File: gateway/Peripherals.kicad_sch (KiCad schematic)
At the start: 11 parts, among them X1101 I2C, X1102 I2C

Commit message: Working on version 1.0
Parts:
- C1101, C1102: footprint Capacitor_SMD:C_0402_1005Metric -> Capacitor_SMD:C_0805_2012Metric; manf# 04025C104JAT2A -> 08053C104M4T4A; mouser# (none) -> 581-08053C104M4T4A
- R1101: footprint (none) -> Resistor_SMD:R_0805_2012Metric; manf (none) -> Bourns; manf# (none) -> CR0805-FX-1001GLF; mouser# (none) -> 652-CR0805-FX-1001GLF
- R1102: footprint (none) -> Resistor_SMD:R_0805_2012Metric; manf (none) -> Bourns; manf# (none) -> CR0805-JW-103GLF; mouser# (none) -> 652-CR0805-JW-103GLF
- TP1101: footprint (none) -> Testpoints_Kampi:TestPoint_Pad_1.0x1.0mm
- X1101: renamed from X?; footprint (none) -> Connector_USB:USB_C_Receptacle_GCT_USB4110; manf (none) -> GCT; manf# (none) -> USB4110-GF-A; mouser# (none) -> 640-USB4110-GF-A
- X1102: renamed from X?; now left out of the parts list
- X1103: renamed from X1101; now left out of the parts list
- X1104: renamed from X1102; now left out of the parts list
- gave numbers to parts that had none: 2

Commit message: Working on PCB
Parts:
- X1103, X1104: footprint (none) -> Connector_PinHeader_2.54mm:PinHeader_1x02_P2.54mm_Vertical
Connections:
- net GPIO.Num0: now reaches X1102.2 (Pin_2)
- net GPIO.Num1: now reaches X1102.3 (Pin_3)
- net GPIO.Num2: now reaches X1102.4 (Pin_4)
- net GPIO.Num3: now reaches X1102.5 (Pin_5)
- net GPIO.Num4: now reaches X1102.6 (Pin_6)
- net GPIO.Num5: now reaches X1102.7 (Pin_7)
- net GPIO.Num6: now reaches X1102.8 (Pin_8)
- net GPIO.Num7: now reaches X1102.9 (Pin_9)
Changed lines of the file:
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@@
 	)
 	(bus_entry
-		(at 363.22 90.17)
+		(at 355.6 90.17)
 		(size 2.54 2.54)
 		(stroke
@@
 	)
 	(bus_entry
-		(at 363.22 85.09)
+		(at 355.6 85.09)
 		(size 2.54 2.54)
 		(stroke
@@
 	)
 	(bus_entry
-		(at 363.22 87.63)
+		(at 355.6 87.63)
 		(size 2.54 2.54)
 		(stroke
@@
 	)
 	(bus_entry
-		(at 363.22 74.93)
+		(at 355.6 74.93)
 		(size 2.54 2.54)
 		(stroke
@@
 	)
 	(bus_entry
-		(at 363.22 77.47)
+		(at 355.6 77.47)
 		(size 2.54 2.54)
 		(stroke
@@
 	)
 	(bus_entry
-		(at 363.22 80.01)
+		(at 355.6 80.01)
 		(size 2.54 2.54)
 		(stroke
@@
 	)
 	(bus_entry
-		(at 363.22 92.71)
+		(at 355.6 92.71)
 		(size 2.54 2.54)
 		(stroke
@@
 	)
 	(bus_entry
-		(at 363.22 82.55)
+		(at 355.6 82.55)
 		(size 2.54 2.54)
 		(stroke
@@
 	(wire
 		(pts
-			(xy 365.76 92.71) (xy 374.65 92.71)
+			(xy 358.14 92.71) (xy 374.65 92.71)
 		)
 		(stroke
@@
 	(wire
 		(pts
-			(xy 365.76 90.17) (xy 374.65 90.17)
+			(xy 358.14 90.17) (xy 374.65 90.17)
 		)
 		(stroke
@@
 	(wire
 		(pts
-			(xy 365.76 85.09) (xy 374.65 85.09)
+			(xy 358.14 85.09) (xy 374.65 85.09)
 		)
 		(stroke
@@
 	(wire
 		(pts
-			(xy 365.76 80.01) (xy 374.65 80.01)
+			(xy 358.14 80.01) (xy 374.65 80.01)
 		)
 		(stroke
@@
 	(wire
 		(pts
-			(xy 365.76 95.25) (xy 374.65 95.25)
+			(xy 358.14 95.25) (xy 374.65 95.25)
 		)
 		(stroke
@@
 	(wire
 		(pts
-			(xy 365.76 82.55) (xy 374.65 82.55)
+			(xy 358.14 82.55) (xy 374.65 82.55)
 		)
 		(stroke
@@
 	(bus
 		(pts
-			(xy 363.22 73.66) (xy 363.22 92.71)
+			(xy 355.6 73.66) (xy 355.6 92.71)
 		)
 		(stroke
@@
 	(bus
 		(pts
-			(xy 354.33 73.66) (xy 363.22 73.66)
+			(xy 354.33 73.66) (xy 355.6 73.66)
 		)
 		(stroke
@@
 	(wire
 		(pts
-			(xy 365.76 87.63) (xy 374.65 87.63)
+			(xy 358.14 87.63) (xy 374.65 87.63)
 		)
 		(stroke
@@
 	(wire
 		(pts
-			(xy 365.76 77.47) (xy 374.65 77.47)
+			(xy 358.14 77.47) (xy 374.65 77.47)
 		)
 		(stroke
@@
 		)
 	)
+	(label "GPIO.Num6"
+		(at 358.14 92.71 0)
+		(effects
+			(font
+				(size 1.27 1.27)
+			)
+			(justify left bottom)
+		)
+	)
+	(label "GPIO.Num1"
+		(at 358.14 80.01 0)
+		(effects
+			(font
+				(size 1.27 1.27)
+			)
+			(justify left bottom)
+		)
+	)
+	(label "GPIO.Num7"
+		(at 358.14 95.25 0)
+		(effects
+			(font
+				(size 1.27 1.27)
+			)
+			(justify left bottom)
+		)
+	)
 	(label "I2C.SCL"
 		(at 358.14 149.86 0)
@@
 		)
 	)
+	(label "GPIO.Num2"
+		(at 358.14 82.55 0)
+		(effects
+			(font
+				(size 1.27 1.27)
+			)
+			(justify left bottom)
+		)
+	)
 	(label "USB.VBUS"
 		(at 144.78 226.06 180)
@@
 		)
 	)
+	(label "GPIO.Num4"
+		(at 358.14 87.63 0)
+		(effects
+			(font
+				(size 1.27 1.27)
+			)
+			(justify left bottom)
+		)
+	)
 	(label "I2C.SCL"
 		(at 353.06 218.44 0)
@@
 		)
 	)
+	(label "GPIO.Num3"
+		(at 358.14 85.09 0)
+		(effects
+			(font
+				(size 1.27 1.27)
+			)
+			(justify left bottom)
+		)
+	)
+	(label "GPIO.Num0"
+		(at 358.14 77.47 0)
+		(effects
+			(font
+				(size 1.27 1.27)
+			)
+			(justify left bottom)
+		)
+	)
 	(label "USB.D_N"
 		(at 144.78 245.11 180)
@@
 		)
 	)
+	(label "GPIO.Num5"
+		(at 358.14 90.17 0)
+		(effects
+			(font
+				(size 1.27 1.27)
+			)
+			(justify left bottom)
+		)
+	)
 	(label "I2C.SDA"
 		(at 358.14 147.32 0)
@@
 		)
 	)
-	(hierarchical_label "I2C{SDA SCL}"
+	(hierarchical_label "I2C{I2C}"
 		(shape bidirectional)
 		(at 354.33 143.51 180)
@@
 		)
 	)
-	(hierarchical_label "GPIO {GPIO}"
+	(hierarchical_label "GPIO{GPIO}"
 		(shape bidirectional)
 		(at 354.33 73.66 180)
@@
 		)
 	)
-	(hierarchical_label "I2C{SDA SCL}"
+	(hierarchical_label "I2C{I2C}"
 		(shape bidirectional)
 		(at 349.25 209.55 180)
@@
 		)
 	)
-	(hierarchical_label "I2C{SDA SCL}"
+	(hierarchical_label "I2C{I2C}"
 		(shape bidirectional)
 		(at 354.33 119.38 180)
@@
 			)
 		)
-		(property "Footprint" ""
+		(property "Footprint" "Connector_PinHeader_2.54mm:PinHeader_1x02_P2.54mm_Vertical"
 			(at 379.73 147.32 0)
 			(hide yes)
@@
 			)
 		)
-		(property "Footprint" ""
+		(property "Footprint" "Connector_PinHeader_2.54mm:PinHeader_1x02_P2.54mm_Vertical"
 			(at 379.73 123.19 0)
 			(hide yes)

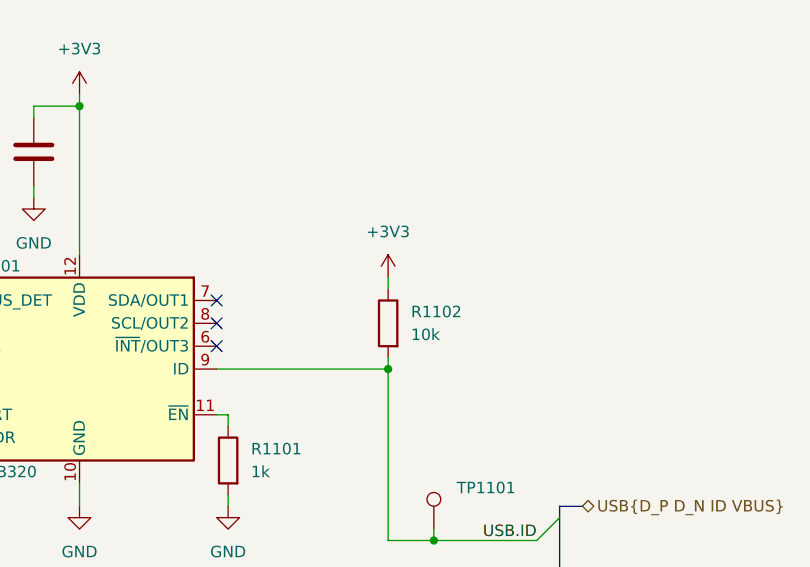
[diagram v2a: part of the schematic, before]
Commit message: Fix broken variant variable
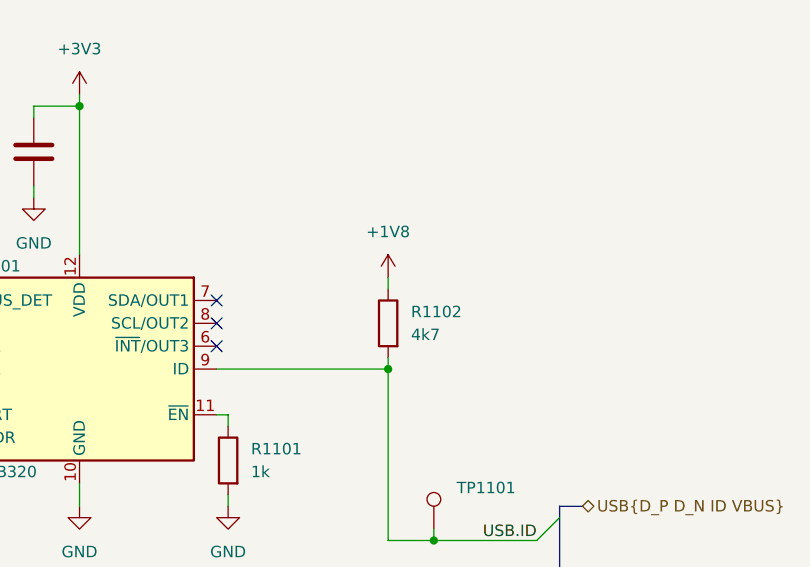
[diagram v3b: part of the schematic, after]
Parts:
- R1102: value 10k -> 4k7; manf# CR0805-JW-103GLF -> CR0805-JW-472ELF; mouser# 652-CR0805-JW-103GLF -> 652-CR0805-JW-472ELF
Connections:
- net +3V3: no longer R1102.1
- new net +1V8: R1102.1
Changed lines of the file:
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@@
 			)
 		)
-		(property "Value" "10k"
+		(property "Value" "4k7"
 			(at 130.81 196.8499 0)
 			(show_name no)
@@
 			)
 		)
-		(property "manf#" "CR0805-JW-103GLF"
+		(property "manf#" "CR0805-JW-472ELF"
 			(at 128.27 195.58 0)
 			(hide yes)
@@
 			)
 		)
-		(property "mouser#" "652-CR0805-JW-103GLF"
+		(property "mouser#" "652-CR0805-JW-472ELF"
 			(at 128.27 195.58 0)
 			(hide yes)
@@
 				(path "/d5742f03-3b1a-42e5-a384-018bd4b919aa/c5103ceb-5325-4a84-a025-9638a412984e/80a97db3-ff4e-4b40-a5b0-8dd5c51e4d83"
 					(reference "#PWR01113")
+					(unit 1)
+				)
+			)
+		)
+	)
+	(symbol
+		(lib_id "power:+1V8")
+		(at 128.27 190.5 0)
+		(unit 1)
+		(body_style 1)
+		(exclude_from_sim no)
+		(in_bom yes)
+		(on_board yes)
+		(in_pos_files yes)
+		(dnp no)
+		(fields_autoplaced yes)
+		(property "Reference" "#PWR01107"
+			(at 128.27 194.31 0)
+			(hide yes)
+			(show_name no)
+			(do_not_autoplace no)
+			(effects
+				(font
+					(size 1.27 1.27)
+				)
+			)
+		)
+		(property "Value" "+1V8"
+			(at 128.27 185.42 0)
+			(show_name no)
+			(do_not_autoplace no)
+			(effects
+				(font
+					(size 1.27 1.27)
+				)
+			)
+		)
+		(property "Footprint" ""
+			(at 128.27 190.5 0)
+			(hide yes)
+			(show_name no)
+			(do_not_autoplace no)
+			(effects
+				(font
+					(size 1.27 1.27)
+				)
+			)
+		)
+		(property "Datasheet" ""
+			(at 128.27 190.5 0)
+			(hide yes)
+			(show_name no)
+			(do_not_autoplace no)
+			(effects
+				(font
+					(size 1.27 1.27)
+				)
+			)
+		)
+		(property "Description" "Power symbol creates a global label with name \"+1V8\""
+			(at 128.27 190.5 0)
+			(hide yes)
+			(show_name no)
+			(do_not_autoplace no)
+			(effects
+				(font
+					(size 1.27 1.27)
+				)
+			)
+		)
+		(pin "1"
+		)
+		(instances
+			(project "Gateway"
+				(path "/d5742f03-3b1a-42e5-a384-018bd4b919aa/c5103ceb-5325-4a84-a025-9638a412984e/80a97db3-ff4e-4b40-a5b0-8dd5c51e4d83"
+					(reference "#PWR01107")
 					(unit 1)
 				)
@@
 					(unit 1)
 				)
-			)
-		)
-	)
-	(symbol
-		(lib_id "power:+3V3")
-		(at 128.27 190.5 0)
-		(unit 1)
-		(body_style 1)
-		(exclude_from_sim no)
-		(in_bom yes)
-		(on_board yes)
-		(in_pos_files yes)
-		(dnp no)
-		(fields_autoplaced yes)
-		(property "Reference" "#PWR01107"
-			(at 128.27 194.31 0)
-			(hide yes)
-			(show_name no)
-			(do_not_autoplace no)
-			(effects
-				(font
-					(size 1.27 1.27)
-				)
-			)
-		)
-		(property "Value" "+3V3"
-			(at 128.27 185.42 0)
-			(show_name no)
-			(do_not_autoplace no)
-			(effects
-				(font
-					(size 1.27 1.27)
-				)
-			)
-		)
-		(property "Footprint" ""
-			(at 128.27 190.5 0)
-			(hide yes)
-			(show_name no)
-			(do_not_autoplace no)
-			(effects
-				(font
-					(size 1.27 1.27)
-				)
-			)
-		)
-		(property "Datasheet" ""
-			(at 128.27 190.5 0)
-			(hide yes)
-			(show_name no)
-			(do_not_autoplace no)
-			(effects
-				(font
-					(size 1.27 1.27)
-				)
-			)
-		)
-		(property "Description" "Power symbol creates a global label with name \"+3V3\""
-			(at 128.27 190.5 0)
-			(hide yes)
-			(show_name no)
-			(do_not_autoplace no)
-			(effects
-				(font
-					(size 1.27 1.27)
-				)
-			)
-		)
-		(pin "1"
-		)
-		(instances
-			(project "Gateway"
-				(path "/d5742f03-3b1a-42e5-a384-018bd4b919aa/c5103ceb-5325-4a84-a025-9638a412984e/80a97db3-ff4e-4b40-a5b0-8dd5c51e4d83"
-					(reference "#PWR01107")
-					(unit 1)
-				)

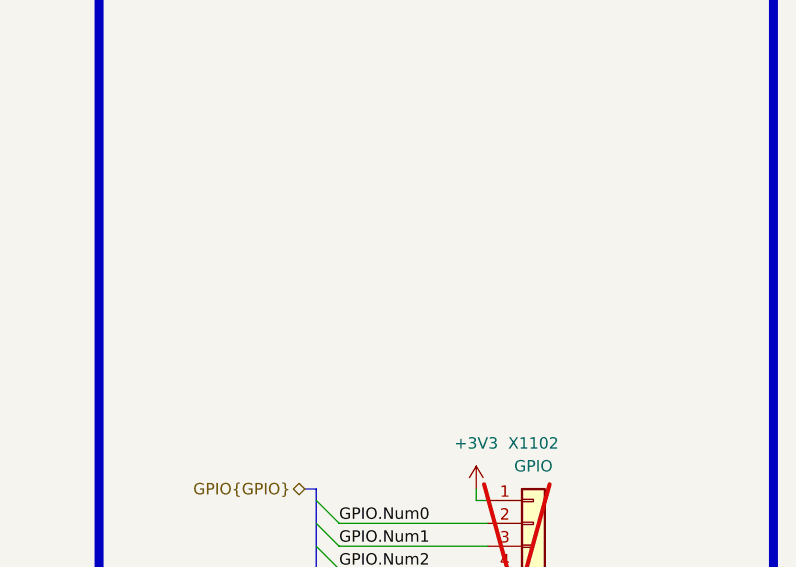
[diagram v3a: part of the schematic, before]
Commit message: Add WiFi antenna, add CAN interface
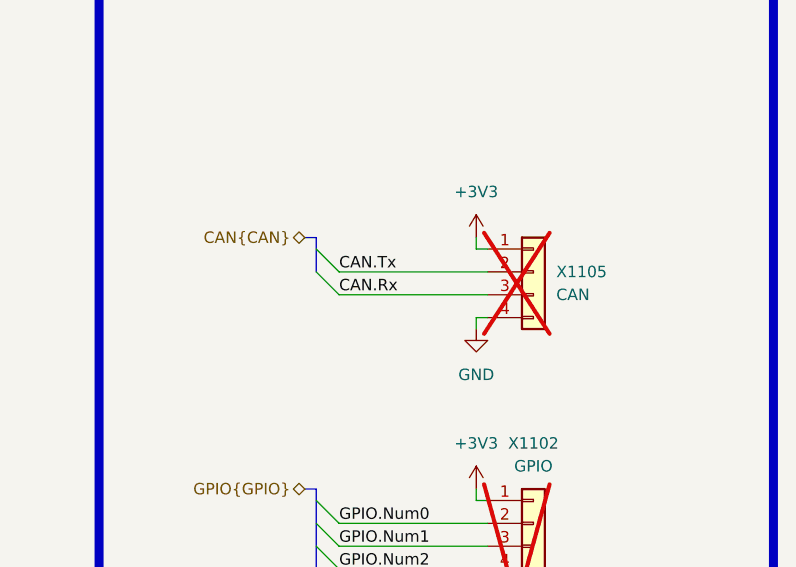
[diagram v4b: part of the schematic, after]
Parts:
- added X1105: CAN, Connector_PinHeader_2.54mm:PinHeader_1x02_P2.54mm_Vertical, symbol Connector_Generic:Conn_01x04
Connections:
- net +3V3: now also X1105.1 (Pin_1)
- net GND: now also X1105.4 (Pin_4)
- new net CAN.Rx: X1105.3 (Pin_3)
- new net CAN.Tx: X1105.2 (Pin_2)

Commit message: Adding level shifter, update documentation
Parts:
- added C1103, C1104, C1105, C1106, C1107, C1108: 100n, Capacitor_SMD:C_0805_2012Metric, symbol Device:C
- added IC1103, IC1104: TXS0102DCU, Package_SO:VSSOP-8_2.3x2mm_P0.5mm, symbol Logic_LevelTranslator:TXS0102DCU
- added IC?: TXB0102DCU, Package_SO:VSSOP-8_2.3x2mm_P0.5mm, symbol Logic_LevelTranslator:TXB0102DCU
- added R1107, R1108, R1109, R1110: 3k3, Resistor_SMD:R_0805_2012Metric, symbol Device:R
- X1105: footprint Connector_PinHeader_2.54mm:PinHeader_1x02_P2.54mm_Vertical -> Connector_Phoenix_MSTB:PhoenixContact_MSTBA_2,5_4-G-5,08_1x04_P5.08mm_Horizontal; manf (none) -> Phoenix Contact; manf# (none) -> 1776524; mouser# (none) -> 651-1776524
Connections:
- net +1V8: now also C1103.1, C1105.1, C1108.1, IC1103.3 (VCCA), IC1103.6 (OE), IC1104.3 (VCCA), IC1104.6 (OE), IC?.3 (VCCA), IC?.6 (OE)
- net +3V3: now also C1104.1, C1106.1, C1107.1, IC1103.7 (VCCB), IC1104.7 (VCCB), IC?.7 (VCCB), R1107.1, R1108.1, R1109.1, R1110.1
- net CAN.Rx: now also IC?.4 (A2); no longer X1105.3 (Pin_3)
- net CAN.Tx: now also IC?.5 (A1); no longer X1105.2 (Pin_2)
- net GND: now also C1103.2, C1104.2, C1105.2, C1106.2, C1107.2, C1108.2, IC1103.2 (GND), IC1104.2 (GND), IC?.2 (GND)
- net I2C.SCL: now also IC1103.4 (A2), IC1104.4 (A2); no longer X1103.3 (Pin_3), X1104.3 (Pin_3)
- net I2C.SDA: now also IC1103.5 (A1), IC1104.5 (A1); no longer X1103.2 (Pin_2), X1104.2 (Pin_2)
- new net: IC?.1 (B2), X1105.3 (Pin_3)
- new net: IC?.8 (B1), X1105.2 (Pin_2)
- new net: IC1104.1 (B2), R1108.2, X1103.3 (Pin_3)
- new net: IC1103.1 (B2), R1110.2, X1104.3 (Pin_3)
- new net: IC1103.8 (B1), R1109.2, X1104.2 (Pin_2)
- new net: IC1104.8 (B1), R1107.2, X1103.2 (Pin_2)
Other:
- moved on the sheet: C1101, C1102, IC1101, IC1102, R1101, R1102, TP1101, X1101, X1102, X1105

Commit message: Replace level shifter, replace CC2530 with CC2652, fix wrong part numbers
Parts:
- removed X1103, X1104: I2C, Connector_PinHeader_2.54mm:PinHeader_1x02_P2.54mm_Vertical, symbol Connector_Generic:Conn_01x04
- added C1409, C1410: 100n, Capacitor_SMD:C_0805_2012Metric, symbol Device:C
- added IC?: TXS0108EPW, Package_SO:TSSOP-20_4.4x6.5mm_P0.65mm, symbol Logic_LevelTranslator:TXS0108EPW
- added R1407: 887k, Resistor_SMD:R_0805_2012Metric, symbol Device:R
- added X1404, X1405: I2C, Connector_Phoenix_MSTB:PhoenixContact_MSTBA_2,5_4-G-5,08_1x04_P5.08mm_Horizontal, symbol Connector_Generic:Conn_01x04
- X1402: renamed from X1102; footprint (none) -> Connector_Phoenix_MSTB:PhoenixContact_MSTBA_2,5_10-G-5,08_1x10_P5.08mm_Horizontal; manf (none) -> Phoenix Contact; manf# (none) -> 1757323; mouser# (none) -> 51-1757323
- gave numbers to parts that had none: 1
- renumbered C1102 to C1401, C1101 to C1402, C1108 to C1403, C1103 to C1404, C1105 to C1405, C1107 to C1406, C1104 to C1407, C1106 to C1408, IC1102 to IC1401, IC1101 to IC1402, IC1104 to IC1404, IC1103 to IC1405, R1101 to R1401, R1102 to R1402, R1107 to R1403, R1109 to R1404, R1108 to R1405, R1110 to R1406, TP1101 to TP1401, X1101 to X1401, X1105 to X1403
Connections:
- net +1V8: now also C1409.1, IC?.10 (OE), IC?.2 (VCCA)
- net +3V3: now also C1410.1, IC?.19 (VCCB), X1404.1 (Pin_1), X1405.1 (Pin_1)
- net GND: now also C1409.2, C1410.2, IC?.11 (GND), X1404.4 (Pin_4), X1405.4 (Pin_4)
- net GPIO.Num0: now also IC?.1 (A1); no longer X1402.2 (Pin_2)
- net GPIO.Num1: now also IC?.3 (A2); no longer X1402.3 (Pin_3)
- net GPIO.Num2: now also IC?.4 (A3); no longer X1402.4 (Pin_4)
- net GPIO.Num3: now also IC?.5 (A4); no longer X1402.5 (Pin_5)
- net GPIO.Num4: now also IC?.6 (A5); no longer X1402.6 (Pin_6)
- net GPIO.Num5: now also IC?.7 (A6); no longer X1402.7 (Pin_7)
- net GPIO.Num6: now also IC?.8 (A7); no longer X1402.8 (Pin_8)
- net GPIO.Num7: now also IC?.9 (A8); no longer X1402.9 (Pin_9)
- net USB.VBUS: now also R1407.1; no longer IC1402.4 (VBUS_DET)
- net at IC1404.1 (B2), R1405.2: now also X1404.3 (Pin_3)
- net at IC1405.1 (B2), R1406.2: now also X1405.3 (Pin_3)
- net at IC1405.8 (B1), R1404.2: now also X1405.2 (Pin_2)
- net at IC1404.8 (B1), R1403.2: now also X1404.2 (Pin_2)
- new net: IC?.20 (B1), X1402.2 (Pin_2)
- new net: IC?.18 (B2), X1402.3 (Pin_3)
- new net: IC?.17 (B3), X1402.4 (Pin_4)
- new net: IC?.16 (B4), X1402.5 (Pin_5)
- new net: IC?.15 (B5), X1402.6 (Pin_6)
- new net: IC?.14 (B6), X1402.7 (Pin_7)
- new net: IC?.13 (B7), X1402.8 (Pin_8)
- new net: IC?.12 (B8), X1402.9 (Pin_9)
- new net: IC1402.4 (VBUS_DET), R1407.2
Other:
- moved on the sheet: X1402
